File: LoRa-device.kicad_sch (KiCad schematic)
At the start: 155 parts, among them J1 Micro_SD_Card_Det1, J3 Conn_01x04_Pin, J4 Conn_01x14_Pin, J6 Conn_01x04_Pin, J8 U.FL, P1 1_25T-1-2A, SW1 EVQPUC02K, SW2 EVQPUC02K, U1 ESP32-S3, U10 TPS2116DRL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

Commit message: Added buttons to case, rehauled power supply.
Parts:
- removed C1: 1uF, Capacitor_SMD:C_0402_1005Metric, symbol Device:C
- removed C12, C21, C50: 22uF, PCM_JLCPCB:C_0603, symbol PCM_JLCPCB-Capacitors:0603,22uF
- removed C2: 10uF, Capacitor_SMD:C_0402_1005Metric, symbol Device:C
- removed C5: 10uF, PCM_JLCPCB:C_0402, symbol PCM_JLCPCB-Capacitors:0402,10uF
- removed C9: 100nF, PCM_JLCPCB:C_0402, symbol PCM_JLCPCB-Capacitors:0402,100nF
- removed D1: LED, LED_SMD:LED_0603_1608Metric, symbol Device:LED
- removed L2: 4.7uH 3V, Inductor_SMD:L_Sunlord_MWSA0402S, symbol Device:L
- removed R15: 1K, Resistor_SMD:R_0402_1005Metric, symbol Device:R
- removed R20: 4.7kΩ, PCM_JLCPCB:R_0402, symbol PCM_JLCPCB-Resistors:0402,4.7kΩ
- removed R32: 100kΩ, PCM_JLCPCB:R_0402, symbol PCM_JLCPCB-Resistors:0402,100kΩ
- removed R33: 8.2kΩ, PCM_JLCPCB:R_0402, symbol PCM_JLCPCB-Resistors:0402,8.2kΩ
- removed R6: 22kΩ, PCM_JLCPCB:R_0402, symbol PCM_JLCPCB-Resistors:0402,22kΩ
- removed TP1: TestPoint, TestPoint:TestPoint_THTPad_1.0x1.0mm_Drill0.5mm, symbol Connector:TestPoint
- removed U10: TPS2116DRL, Package_TO_SOT_SMD:SOT-583-8, symbol Power_Management:TPS2116DRL
- removed U12: MLT-5020, LoRa_library:BUZ-SMD_L5.0-W5.5-P4.60, symbol LoRa_library:MLT-5020
- removed U13: ES8311, LoRa_library:WQFN-20_L3.0-W3.0-P0.40-BL-EP1.7, symbol LoRa_library:ES8311
- removed U16: Black_headphone_jack, LoRa_library:AUDIO-TH_320B, symbol LoRa_library:Black_headphone_jack
- removed U3: TP4055, Package_TO_SOT_SMD:SOT-23-5, symbol Battery_Management:MCP73831-2-OT
- removed U9: AP63203WU, Package_TO_SOT_SMD:TSOT-23-6, symbol Regulator_Switching:AP63203WU
- added C54: 4.7uF, PCM_JLCPCB:C_0402, symbol PCM_JLCPCB-Capacitors:0402,4.7uF
- added C55: 10uF, PCM_JLCPCB:C_0603, symbol PCM_JLCPCB-Capacitors:0603,10uF
- added C56: 22uF, PCM_JLCPCB:C_0603, symbol PCM_JLCPCB-Capacitors:0603,22uF
- added C57: 6.8pF, PCM_JLCPCB:C_0402, symbol PCM_JLCPCB-Capacitors:0402,6.8pF
- added D4, D5: LED, LED_SMD:LED_0603_1608Metric, symbol Device:LED
- added L7: 4.7uH 3V, Inductor_SMD:L_Sunlord_MWSA0402S, symbol Device:L
- added P2: 1_25T-1-2A, LoRa_library:CONN-TH_1.25T-1-2A, symbol LoRa_library:1_25T-1-2A
- added R54, R55: 1K, Resistor_SMD:R_0402_1005Metric, symbol Device:R
- added R56: 150kΩ, PCM_JLCPCB:R_0402, symbol PCM_JLCPCB-Resistors:0402,150kΩ
- added R57: 680kΩ, PCM_JLCPCB:R_0603, symbol PCM_JLCPCB-Resistors:0603,680kΩ
- added U12: TLV62569DBV, Package_TO_SOT_SMD:SOT-23-5, symbol Regulator_Switching:TLV62569DBV
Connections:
- net +3V3: now also C55.1, C56.1, C57.1, D4.2 (A), D5.2 (A), L7.2, R57.1
- net GND: now also C54.2, C55.2, C56.2, R56.2, U12.2 (GND)
- net VSYS_SW: now also C54.1, U12.1 (EN), U12.4 (VIN)
- net GPA1: now reaches R53.2, U7.9 (STAT1)
- net GPA1: now also U14.18 (GPA1), R55.1
- net GPB5: now reaches U14.2 (GPB5)
- net GPB5: now also R52.2, U7.3 (STAT2), R54.1
- net at U19.10 (OUTN): now also P2.2
- net at U19.9 (OUTP): now also P2.1
- new net: D4.1 (K), R54.2
- new net: C57.2, R56.1, R57.2, U12.5 (FB)
- new net: D5.1 (K), R55.2
- new net: L7.1, U12.3 (SW)
- no-connect marks 29 -> 26
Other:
- moved on the sheet: C42, C51, C52, C53, C8, P1, R12, R19, R41, R49, R50, R51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

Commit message: Almost ready for routing, major fixes, case ready.
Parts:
- removed C34: 1uF, PCM_JLCPCB:C_0402, symbol PCM_JLCPCB-Capacitors:0402,1uF
- removed C51: 2.2uF, PCM_JLCPCB:C_0402, symbol PCM_JLCPCB-Capacitors:0402,2.2uF
- removed C52: 10uF, PCM_JLCPCB:C_0402, symbol PCM_JLCPCB-Capacitors:0402,10uF
- removed R50: 330Ω, PCM_JLCPCB:R_0402, symbol PCM_JLCPCB-Resistors:0402,330Ω
- removed R56: 150kΩ, PCM_JLCPCB:R_0402, symbol PCM_JLCPCB-Resistors:0402,150kΩ
- removed R57: 680kΩ, PCM_JLCPCB:R_0603, symbol PCM_JLCPCB-Resistors:0603,680kΩ
- added C1: 2.2uF, PCM_JLCPCB:C_0603, symbol PCM_JLCPCB-Capacitors:0603,2.2uF
- added C2: 10uF, PCM_JLCPCB:C_0603, symbol PCM_JLCPCB-Capacitors:0603,10uF,(2)
- added C5: 4.7uF, PCM_JLCPCB:C_0402, symbol PCM_JLCPCB-Capacitors:0402,4.7uF
- added C9: 100nF, PCM_JLCPCB:C_0402, symbol PCM_JLCPCB-Capacitors:0402,100nF
- added R32: 510Ω, PCM_JLCPCB:R_0402, symbol PCM_JLCPCB-Resistors:0402,510Ω
- added R33: 100kΩ, PCM_JLCPCB:R_0402, symbol PCM_JLCPCB-Resistors:0402,100kΩ
- added R50: 300kΩ, PCM_JLCPCB:R_0603, symbol PCM_JLCPCB-Resistors:0603,300kΩ
- added R56: 150kΩ, PCM_JLCPCB:R_0603, symbol PCM_JLCPCB-Resistors:0603,150kΩ
- MK1: LCSC (none) -> C19272537
- U12: LCSC (none) -> C141836
- U14: LCSC (none) -> C629439
- U19: LCSC (none) -> C910544
- U6: LCSC (none) -> C15999
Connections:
- net +3V3: now also R50.1
- net +5V: now also C1.1
- net GND: now also C1.2, C2.2, C5.2, C9.2, R32.2, R33.2
- net GPA5: now also SW1.3; no longer D3.2 (A)
- net GPA7: now also D3.2 (A); no longer SW1.3
- net LORA_RF_EN: now also U14.4 (GPB7); no longer U14.27 (GPB2)
- net VSYS: now also C2.1
- net at C57.2, U12.5 (FB): now also R33.1, R56.2
- net at U18.6 (V_BCKP), U4.5 (OUT): now also C5.1, C9.1
- net at U7.8 (ISET): now also R32.1
- net GPB7 renamed GPB2
- net GPB2: now also U14.27 (GPB2); no longer U14.4 (GPB7)
- new net: R50.2, R56.1

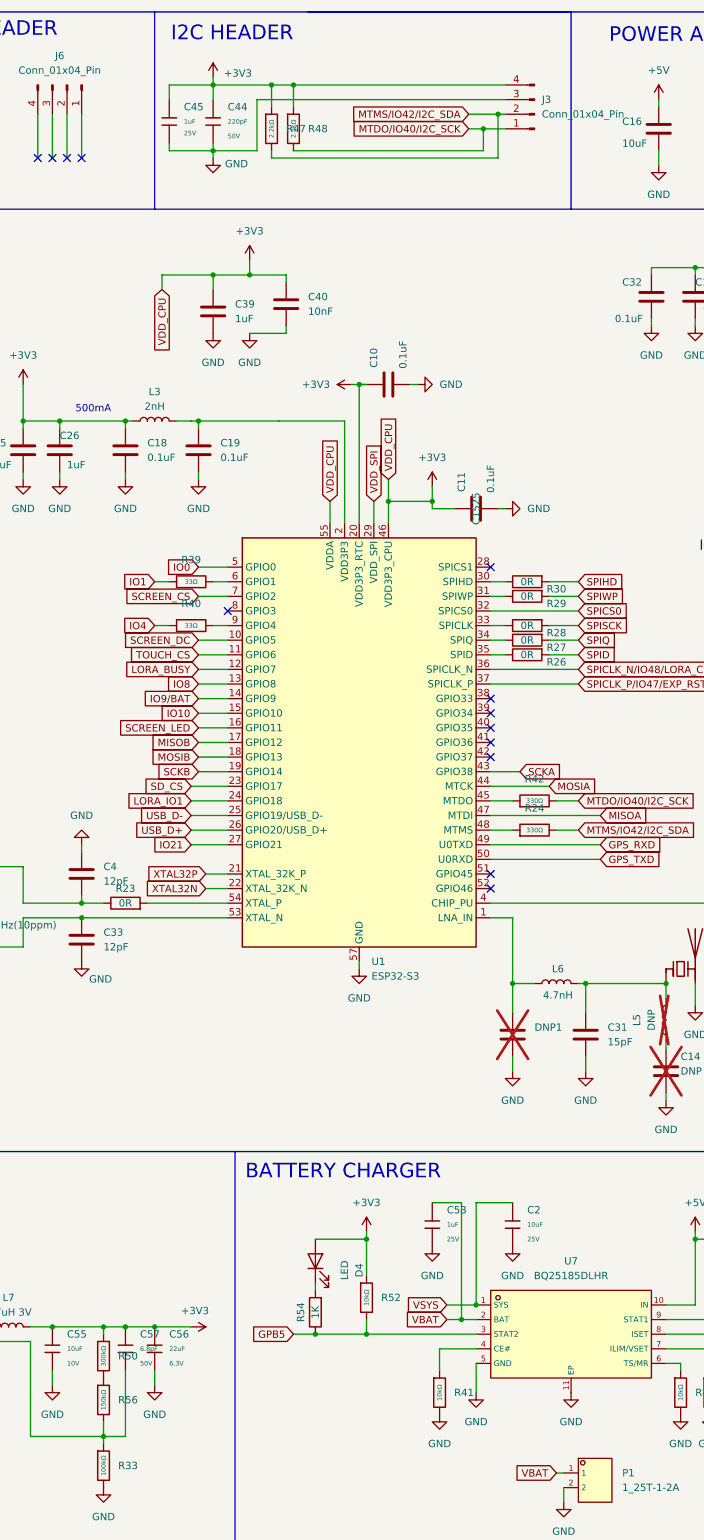
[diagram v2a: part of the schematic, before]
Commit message: Case prototype ready. Added thermal pads.
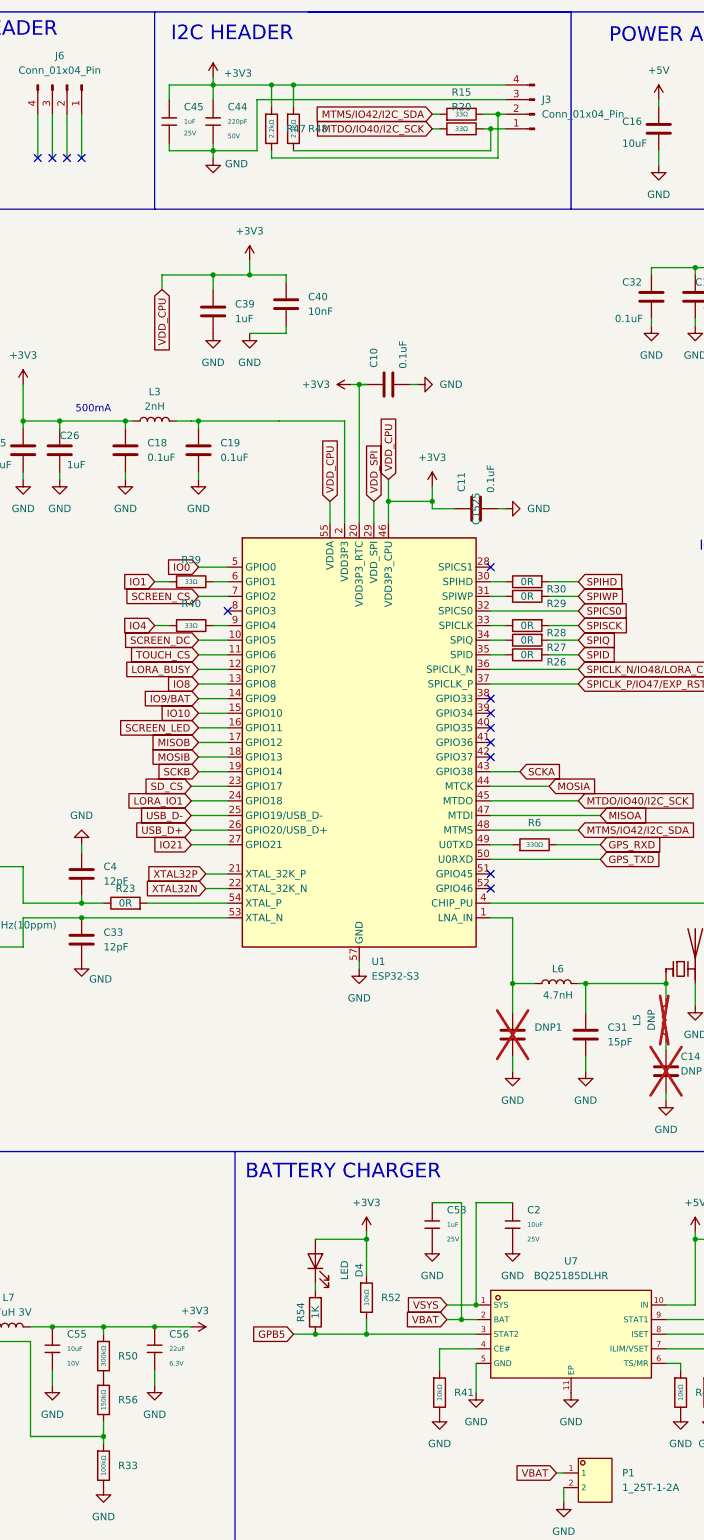
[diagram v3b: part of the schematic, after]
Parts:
- removed C57: 6.8pF, PCM_JLCPCB:C_0402, symbol PCM_JLCPCB-Capacitors:0402,6.8pF
- removed R24, R42: 330Ω, PCM_JLCPCB:R_0402, symbol PCM_JLCPCB-Resistors:0402,330Ω
- added R15, R20: 33Ω, PCM_JLCPCB:R_0402, symbol PCM_JLCPCB-Resistors:0402,33Ω
- added R6: 330Ω, PCM_JLCPCB:R_0402, symbol PCM_JLCPCB-Resistors:0402,330Ω
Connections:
- net GPS_RXD: now also R6.2; no longer U1.49 (U0TXD)
- net MTDO/IO40/I2C_SCK: now also U1.45 (MTDO), R20.1; no longer J3.1 (Pin_1), R48.2
- net MTMS/IO42/I2C_SDA: now also U1.48 (MTMS), R15.1; no longer J3.2 (Pin_2), R47.2
- new net: J3.1 (Pin_1), R20.2, R48.2
- new net: R6.1, U1.49 (U0TXD)
- new net: J3.2 (Pin_2), R15.2, R47.2

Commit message: Ready for routing!
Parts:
- removed DNP1: ~, Capacitor_SMD:C_0402_1005Metric, symbol Device:C
- removed L4: 68nH,300mA, PCM_JLCPCB:L_0603, symbol PCM_JLCPCB-Inductors:68nH,300mA
- added C12: 1.4pF, Capacitor_SMD:C_0402_1005Metric, symbol Device:C
- added JP1: Jumper_2_Open, Jumper:SolderJumper-2_P1.3mm_Open_RoundedPad1.0x1.5mm, symbol Jumper:Jumper_2_Open
- added L2: 68nH, Inductor_SMD:L_0402_1005Metric, symbol Device:L
- C31: value 15pF -> 1.4pF; LCSC C1548 -> C2181496; MNF PART NUMBER C1548 -> C2181496
- L3: LCSC C77103 -> C18216; MNF PART NUMBER C77103 -> C18216
- L6: value 4.7nH -> 2.7nH; LCSC C13595 -> C27123; MNF PART NUMBER C13595 -> C27123
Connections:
- net GND: now also C12.2
- net MISOA: now also J4.13 (Pin_13); no longer J1.7 (DAT0), R14.2
- net MISOB: now also J1.7 (DAT0), R14.2, JP1.1 (A); no longer J4.13 (Pin_13), J4.9 (Pin_9)
- net MOSIA: now also J4.12 (Pin_12); no longer J1.3 (CMD)
- net MOSIB: now also J1.3 (CMD); no longer J4.12 (Pin_12)
- net SCKA: now also J4.10 (Pin_10); no longer J1.5 (CLK)
- net SCKB: now also J1.5 (CLK); no longer J4.10 (Pin_10)
- net at C28.1, C29.1, R36.1: now also L2.1
- net at C27.2, J8.1 (In): now also L2.2
- net at L6.1, U1.1 (LNA_IN): now also C12.1
- new net: J4.9 (Pin_9), JP1.2 (B)
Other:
- moved on the sheet: L6

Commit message: Routing started
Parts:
- removed JP1: Jumper_2_Open, Jumper:SolderJumper-2_P1.3mm_Open_RoundedPad1.0x1.5mm, symbol Jumper:Jumper_2_Open
- added H1, H2, H3, H4: MountingHole, MountingHole:MountingHole_3mm, symbol Mechanical:MountingHole
- added R24: 0R, Resistor_SMD:R_0402_1005Metric, symbol Device:R
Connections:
- net MISOB: now also R24.1
- net at J4.9 (Pin_9): now also R24.2

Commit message: More routing, modifying case buttons and locking
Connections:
- net GPS_WKUP: now also U14.17 (GPA0); no longer U14.21 (GPA4)
- net LORA_IO1: now also U1.10 (GPIO5); no longer U1.24 (GPIO18)
- net LORA_IO2: now also U14.26 (GPB1); no longer U14.25 (GPB0)
- net LORA_IO3: now also U14.25 (GPB0); no longer U14.26 (GPB1)
- net LORA_RF_EN: now also U14.24 (GPA7); no longer U14.4 (GPB7)
- net LORA_RST: now also U14.21 (GPA4); no longer U14.17 (GPA0)
- net SCREEN_CS: now also U1.24 (GPIO18); no longer U1.7 (GPIO2)
- net SCREEN_DC: now also U1.23 (GPIO17); no longer U1.10 (GPIO5)
- net GPA7 renamed GPB7
- net GPB7: now also U14.4 (GPB7); no longer U14.24 (GPA7)
- net SD_CS renamed SPICLK_N/IO48/SD_CS
- net SPICLK_N/IO48/SD_CS: now also U1.36 (SPICLK_N); no longer U1.23 (GPIO17)
- net SPICLK_N/IO48/LORA_CS renamed LORA_CS
- net LORA_CS: now also U1.7 (GPIO2); no longer U1.36 (SPICLK_N)

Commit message: Minor component changes.
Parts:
- removed C17: 10uF, Capacitor_SMD:C_0402_1005Metric, symbol Device:C
- removed C49: 10uF, PCM_JLCPCB:C_0402, symbol PCM_JLCPCB-Capacitors:0402,10uF
- removed L7: 4.7uH 3V, Inductor_SMD:L_Sunlord_MWSA0402S, symbol Device:L
- removed MK1: SPH0645LM4H, Sensor_Audio:Knowles_SPH0645LM4H-6_3.5x2.65mm, symbol Sensor_Audio:SPH0645LM4H
- removed R39, R40: 33Ω, PCM_JLCPCB:R_0402, symbol PCM_JLCPCB-Resistors:0402,33Ω
- added C21: 100nF, PCM_JLCPCB:C_0402, symbol PCM_JLCPCB-Capacitors:0402,100nF
- added U3: ICS-43432, LoRa_library:SENSOR-SMD_ICS-43432, symbol LoRa_library:ICS-43432
- added U9: MHCI04020-2R2M-R8, LoRa_library:IND-SMD_L4.6-W4.1, symbol LoRa_library:MHCI04020-2R2M-R8
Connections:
- net +3V3: now also C21.1, U3.3 (VDD), U9.2
- net GND: now also C21.2, U3.1 (LR), U3.2 (CONFIG), U3.4 (GND)
- net IO1: now also U1.6 (GPIO1), U3.5 (WS)
- net IO4: now also U1.9 (GPIO4), U3.6 (SCK)
- net at R1.1, R43.1: now also U3.7 (SD)
- net at U12.3 (SW): now also U9.1
- net AUDIO_OUTP: now reaches P2.1, U19.9 (OUTP)
- net AUDIO_OUTN: now reaches P2.2, U19.10 (OUTN)
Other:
- moved on the sheet: C56, R1, R43

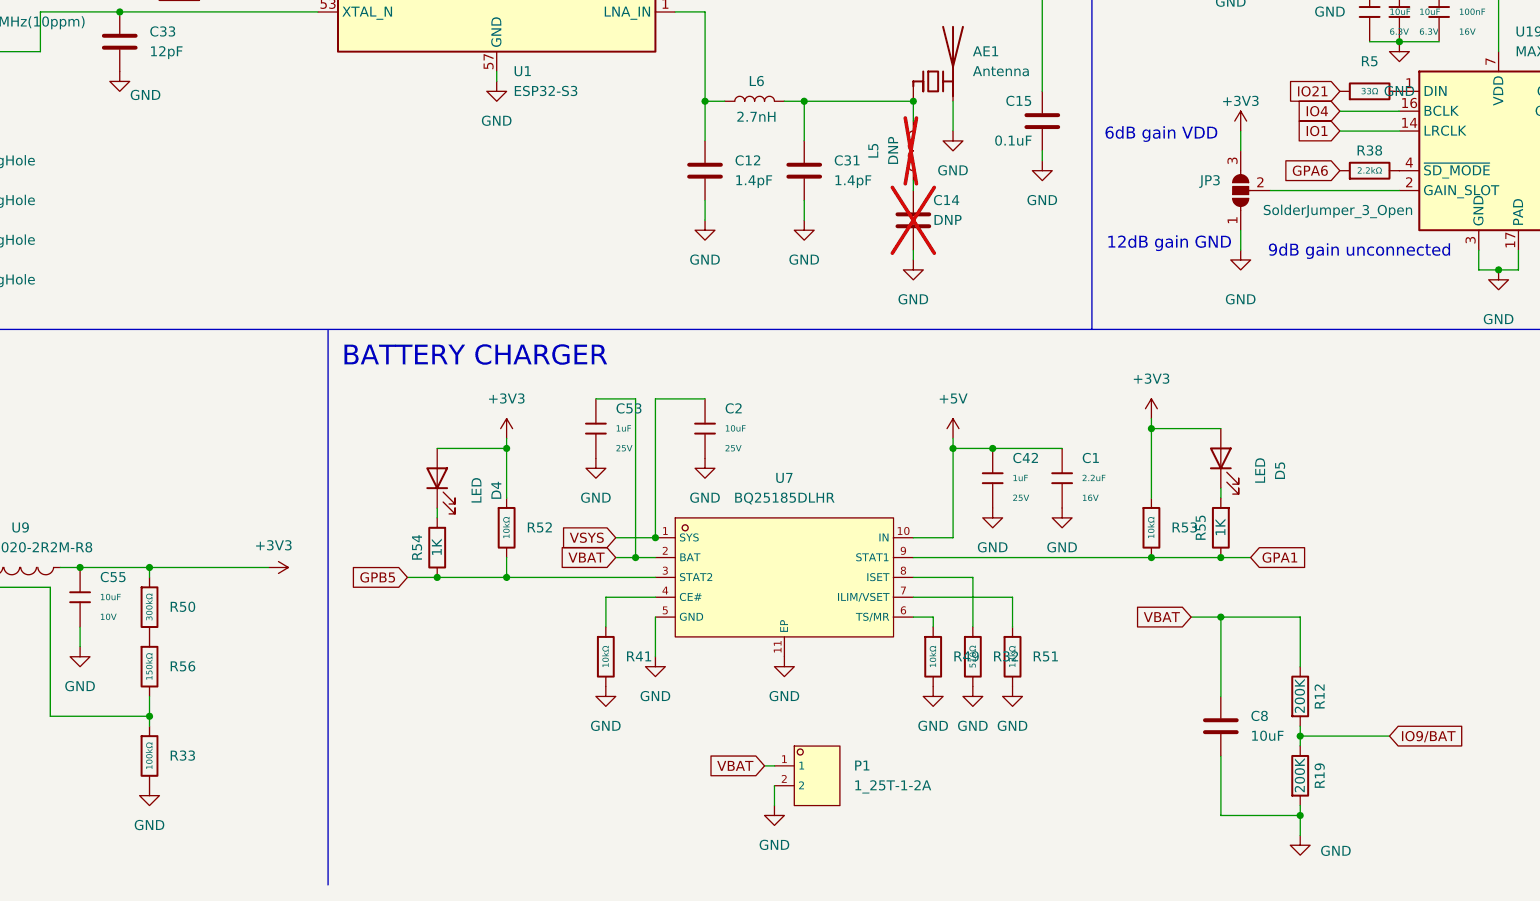
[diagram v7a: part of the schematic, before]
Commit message: Perfected 3V3 routing
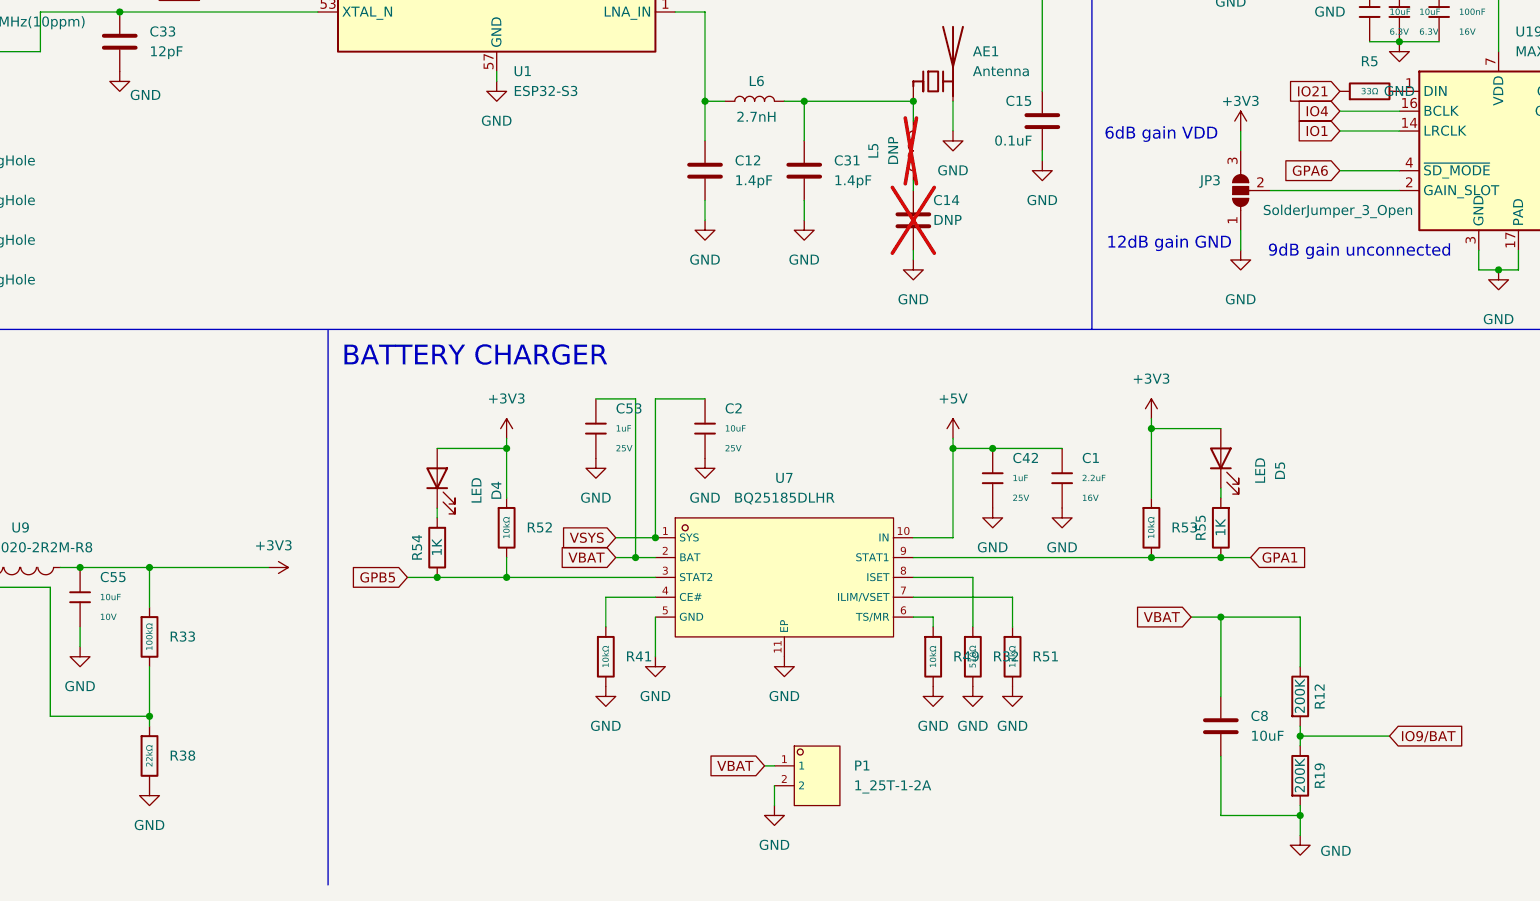
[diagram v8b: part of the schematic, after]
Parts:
- removed R38: 2.2kΩ, PCM_JLCPCB:R_0402, symbol PCM_JLCPCB-Resistors:0402,2.2kΩ
- removed R50: 300kΩ, PCM_JLCPCB:R_0603, symbol PCM_JLCPCB-Resistors:0603,300kΩ
- removed R56: 150kΩ, PCM_JLCPCB:R_0603, symbol PCM_JLCPCB-Resistors:0603,150kΩ
- added R38: 22kΩ, PCM_JLCPCB:R_0402, symbol PCM_JLCPCB-Resistors:0402,22kΩ
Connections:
- net +3V3: now also R33.1
- net GND: now also R38.2; no longer R33.2
- net GPA6: now also U19.4 (~{SD_MODE})
- net at U12.5 (FB): now also R33.2, R38.1; no longer R33.1
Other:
- moved on the sheet: R33
